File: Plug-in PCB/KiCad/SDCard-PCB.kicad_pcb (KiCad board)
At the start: 6 copper layers, 43 x 40 mm, 74 parts, among them J1 Conn_Coaxial, J10 Conn_01x01, J11 Conn_01x01, J14 Conn_01x01, J15 Conn_01x08, J16 Conn_01x01, J18 Conn_01x08, J2 Conn_01x01, J3 Conn_01x01, J4 Conn_01x01, J5 Conn_01x01, J6 Conn_01x01, J7 Conn_01x01, J8 Conn_01x01, J9 Conn_01x01, U1 DS90UB933-Q1, U2 TPS62402-Q1, U4 ATSAME70N21A-CN, Y1 ABM8G-12.000MHZ-4Y-T3

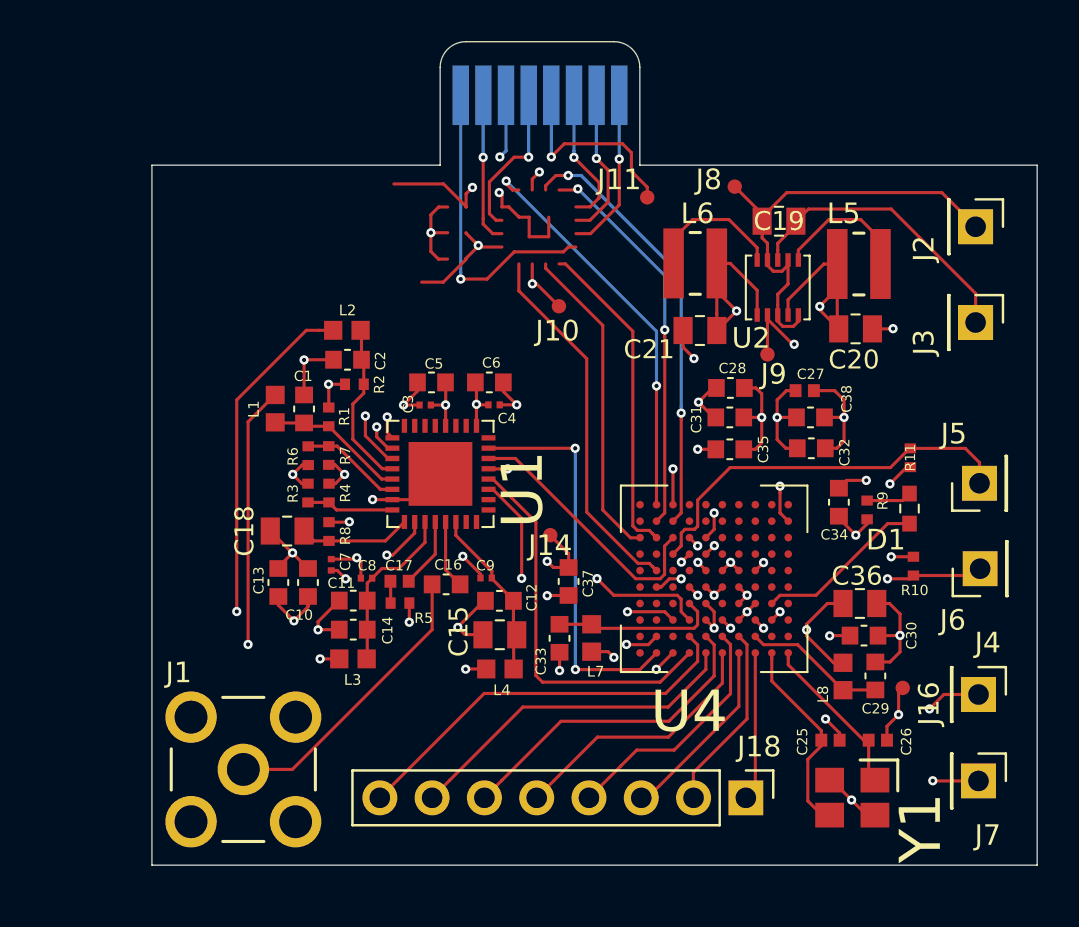
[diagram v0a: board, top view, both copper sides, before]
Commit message: Wired Expansion Board Update
1. Begin hardcoding bit-bang communication between wirefree MCU and wired expansion MCU.
++ Can I use the PIO module on the pins to send data in sync while grabbing image from the sensor with parallel capture mode?

2. Wired expansion board schematics and layout modifications
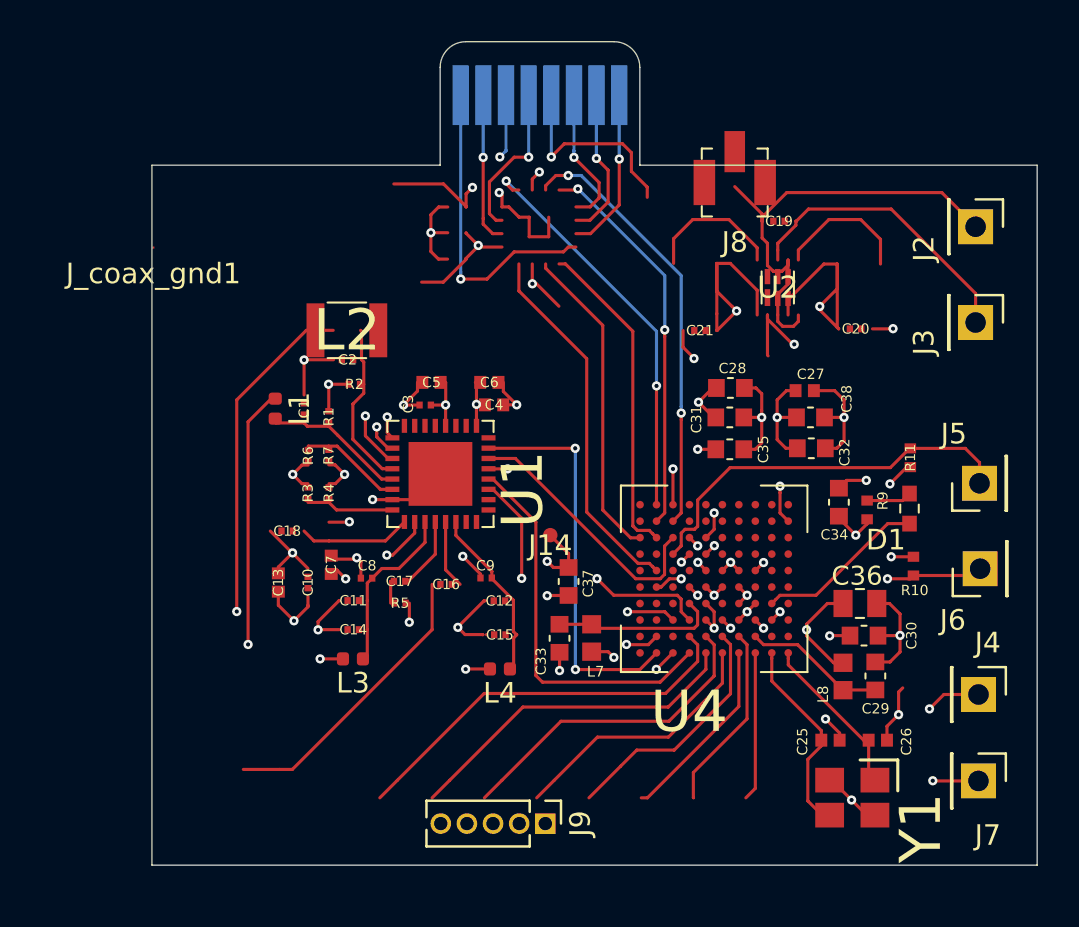
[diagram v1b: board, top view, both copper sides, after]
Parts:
- removed J1: Conn_Coaxial, .Connector:SMA-J-P-H-RA-TH1
- removed J10, J11, J16: Conn_01x01, .Connector:Conn_1x1_700_Circular_Pad
- removed J18: Conn_01x08, Connector_PinHeader_2.54mm:PinHeader_1x08_P2.54mm_Vertical
- removed L5, L6: VLS3012HBX-2R2M, .Inductor:VLS3012HBX-2R2M
- removed R8: 10k, .Resistor:R_0402_1005Metric_ERJ_L
- added J_coax_gnd1: Conn_01x01, .Connector:Conn_1x1_100x100_Pad, F.Cu at (100.1, 57.0)
- C1: value GQM1875C2E101JB12D -> GRM033R61A104ME15D; footprint .Capacitor:C_0603_1608Metric_L -> .Capacitor:C_0201_0603Metric_L
- C10, C11, C12: value GCJ188R71E104KA12D -> GRM033R61A104ME15D; footprint .Capacitor:C_0603_1608Metric_L -> .Capacitor:C_0201_0603Metric_L
- C13: value GRM188R61E475KE11D -> GRM155R60J106ME15D; footprint .Capacitor:C_0603_1608Metric_L -> .Capacitor:C_0402_1005Metric_L
- C14: value GRM188R61E475KE11D -> GRM033R71A103KA01D; footprint .Capacitor:C_0603_1608Metric_L -> .Capacitor:C_0201_0603Metric_L
- C15: value GRM21BR61C226ME44L -> GRM033R71A103KA01D; footprint .Capacitor:C_0805_2012Metric_L -> .Capacitor:C_0201_0603Metric_L
- C16: value GCJ188R71E104KA12D -> GRM033R71A103KA01D; footprint .Capacitor:C_0603_1608Metric_L -> .Capacitor:C_0201_0603Metric_L
- C17: value GRM155R71E473KA88D -> GRM033R71A103KA01D; footprint .Capacitor:C_0402_1005Metric_L -> .Capacitor:C_0201_0603Metric_L
- C18: value GCM21BR71E105KA56L -> GRM033R71A103KA01D; footprint .Capacitor:C_0805_2012Metric_L -> .Capacitor:C_0201_0603Metric_L
- C19: value GRM21BR61E106MA73L -> GRM033R61A105ME15D; footprint .Capacitor:C_0805_2012Metric_L -> .Capacitor:C_0201_0603Metric_L
- C2: value GQM1875C2E101JB12D -> GRM033R61C473KE84D; footprint .Capacitor:C_0603_1608Metric_L -> .Capacitor:C_0201_0603Metric_L
- C20, C21: value GRM21BR61C226ME44L -> GRM033R61A105ME15D; footprint .Capacitor:C_0805_2012Metric_L -> .Capacitor:C_0201_0603Metric_L
- C3: value GRM033R71A103KA01D -> GRM033R61A105ME15D
- C4: value GRM033R71A103KA01D -> GRM155R60J475ME47D; footprint .Capacitor:C_0201_0603Metric_L -> .Capacitor:C_0402_1005Metric_L
- C5: value GCJ188R71E104KA12D -> GRM155R60J475ME47D; footprint .Capacitor:C_0603_1608Metric_L -> .Capacitor:C_0402_1005Metric_L
- C6: value GCJ188R71E104KA12D -> GRJ155R60J106ME11D; footprint .Capacitor:C_0603_1608Metric_L -> .Capacitor:C_0402_1005Metric_L
- C7: value GRM033R71A103KA01D -> GRM155R60J106ME15D; footprint .Capacitor:C_0201_0603Metric_L -> .Capacitor:C_0402_1005Metric_L
- C8, C9: value GRM033R71A103KA01D -> GRM033R61A104ME15D
- J8: value Conn_01x01 -> Conn_Coaxial; footprint .Connector:Conn_1x1_700_Circular_Pad -> .Connector:U_FL-R-SMT_10_
- J9: value Conn_01x01 -> Conn_01x05; footprint .Connector:Conn_1x1_700_Circular_Pad -> Connector_PinHeader_1.27mm:PinHeader_1x05_P1.27mm_Vertical
- L1, L3, L4: value 1k @ 100MHz -> BLM15HD102SN1D; footprint .Inductor:L_0603_1608Metric_L -> Inductor_SMD:L_0402_1005Metric
- L2: value 1k @ 100MHz -> ADL3225V-470MT-TL000; footprint .Inductor:L_0603_1608Metric_L -> .Inductor:L_1210_3225Metric_L
- R1: value 4.7k -> ERJ-1GEF49R9C; footprint .Resistor:R_0402_1005Metric_ERJ_L -> .Resistor:R_0201_0603Metric_ERJ_L
- R2: value 4.7k -> ERJ-1GEF3321C; footprint .Resistor:R_0402_1005Metric_ERJ_L -> .Resistor:R_0201_0603Metric_ERJ_L
- R3: value 10 -> ERJ-1GEF1002C; footprint .Resistor:R_0402_1005Metric_ERJ_L -> .Resistor:R_0201_0603Metric_ERJ_L
- R4: value 50 or 4.7 -> ERJ-1GEF1003C; footprint .Resistor:R_0402_1005Metric_ERJ_L -> .Resistor:R_0201_0603Metric_ERJ_L
- R5: value 50 -> ERJ-1GEF1002C; footprint .Resistor:R_0402_1005Metric_ERJ_L -> .Resistor:R_0201_0603Metric_ERJ_L
- R6: value open -> ERJ-1GEF3321C; footprint .Resistor:R_0402_1005Metric_ERJ_L -> .Resistor:R_0201_0603Metric_ERJ_L
- R7: value 0 -> MMBT3904LP-7B; footprint .Resistor:R_0402_1005Metric_ERJ_L -> .Resistor:R_0201_0603Metric_ERJ_L
- U2: value TPS62402-Q1 -> TLV7103318DSER; footprint .Package_SON:SON_10_P50_300X300X100L40X24L -> .Package_SON:SON_6_P50_150X150X80L50X25L
- moved J9 25.2 mm to (119.1, 85.0), turned to 270 degrees
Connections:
- net /OnBoardMCU/CLK_OUT renamed Net-(U4-PadJ3)
- net /OnBoardMCU/IR_Receiver renamed Net-(U4-PadC1)
- net /OnBoardMCU/LED_PWM renamed Net-(U4-PadD8)
- net /OnBoardMCU/MONITOR0 renamed Net-(U4-PadG2)
- net /OnBoardMCU/NRESET renamed Net-(U4-PadG10)
- net /OnBoardMCU/RESET_N renamed Net-(U4-PadE2)
- net /OnBoardMCU/TRIGGER0 renamed Net-(U4-PadH1)
- net /OnBoardMCU/img_d6 renamed Net-(U4-PadK10)
- net /OnBoardMCU/img_d7 renamed Net-(U4-PadG5)
- net Net-(R3-Pad2) renamed /Serializer/MODE
- net Net-(U1-Pad24) renamed /Serializer/IMG_out5
- net Net-(U1-Pad26) renamed /Serializer/IMG_out6
- net Net-(U1-Pad27) renamed /Serializer/IMG_out7
- net Net-(U4-PadB10) renamed /OnBoardMCU/img_out3
- net Net-(U4-PadE10) renamed /OnBoardMCU/img_out0
- net Net-(U4-PadE8) renamed /OnBoardMCU/img_out1
- net Net-(U4-PadF10) renamed /OnBoardMCU/img_out2
- net Net-(U4-PadG9) renamed /OnBoardMCU/img_out4
- net Net-(U4-PadJ10) renamed /OnBoardMCU/img_out5
- net Net-(U4-PadK4) renamed /OnBoardMCU/img_out7
- net Net-(U4-PadK6) renamed /OnBoardMCU/img_out6
- C1 pad 1: Net-(C1-Pad1) -> /Serializer/DOUT_P
- C1 pad 2: Earth -> Net-(C1-Pad2)
- C10 pad 1: +1V8 -> /Serializer/VDDCML
- C10 pad 2: Earth -> GND
- C11 pad 1: Net-(C11-Pad1) -> +1V8
- C11 pad 2: Earth -> GND
- C12 pad 1: Net-(C12-Pad1) -> +1V8
- C12 pad 2: Earth -> GND
- C13 pad 1: +1V8 -> +5V
- C13 pad 2: Earth -> GND
- C14 pad 1: Net-(C11-Pad1) -> +1V8
- C14 pad 2: Earth -> GND
- C15 pad 1: Net-(C12-Pad1) -> /Serializer/VDDPLL
- C15 pad 2: Earth -> GND
- C16 pad 1: Net-(C16-Pad1) -> /Serializer/VDDCML
- C16 pad 2: Net-(C16-Pad2) -> GND
- C17 pad 1: Net-(C17-Pad1) -> +1V8
- C17 pad 2: Net-(C17-Pad2) -> GND
- C18 pad 1: Net-(C18-Pad1) -> +1V8
- C18 pad 2: Earth -> GND
- C19 pad 1: +BATT -> +5V
- C19 pad 2: Earth -> GND
- C2 pad 2: Earth -> Net-(C2-Pad2)
- C20 pad 2: Earth -> GND
- C21 pad 2: Earth -> GND
- C3 pad 1: +1V8 -> /Serializer/PDB
- C3 pad 2: Earth -> GND
- C4 pad 1: +3V3 -> +1V8
- C4 pad 2: Earth -> GND
- C5 pad 1: +1V8 -> /Serializer/VDDPLL
- C5 pad 2: Earth -> GND
- C6 pad 1: +3V3 -> /Serializer/VDDCML
- C6 pad 2: Earth -> GND
- C7 pad 1: +1V8 -> +5V
- C7 pad 2: Earth -> GND
- C8 pad 1: Net-(C11-Pad1) -> +1V8
- C8 pad 2: Earth -> GND
- C9 pad 1: Net-(C12-Pad1) -> /Serializer/VDDPLL
- C9 pad 2: Earth -> GND
- J15 pad 1: /SD_Input/DAT2 -> /SD_Input/SD_in2
- J15 pad 2: /SD_Input/DAT3 -> /SD_Input/SD_in3
- J15 pad 3: /SD_Input/SDCardCMDA -> /SD_Input/WXB_CMD
- J15 pad 4: +3V3 -> Net-(J15-Pad4)
- J15 pad 5: /SD_Input/SDCardCLKA -> /SD_Input/WXB_CLK
- J15 pad 7: /SD_Input/DAT0 -> /SD_Input/SD_in0
- J15 pad 8: /SD_Input/DAT1 -> /SD_Input/SD_in1
- J8 pad 1: +BATT -> /Serializer/DOUT_P
- J9 pad 1: Earth -> /OnBoardMCU/test1
- L1 pad 1: /OnBoardMCU/SDA -> /Serializer/DOUT_P
- L1 pad 2: Net-(C1-Pad1) -> Net-(L1-Pad2)
- L2 pad 1: /OnBoardMCU/SCL -> Net-(L1-Pad2)
- L2 pad 2: Net-(C2-Pad1) -> +5V
- L3 pad 1: Net-(C11-Pad1) -> /Serializer/VDDPLL
- L4 pad 1: Net-(C12-Pad1) -> /Serializer/VDDCML
- R1 pad 1: +1V8 -> GND
- R1 pad 2: Net-(C1-Pad1) -> Net-(C2-Pad1)
- R2 pad 1: +1V8 -> +3V3
- R2 pad 2: Net-(C2-Pad1) -> /OnBoardMCU/SCL
- R4 pad 2: Earth -> GND
- R5 pad 1: Net-(C17-Pad1) -> +1V8
- R5 pad 2: Earth -> /Serializer/PDB
- R6 pad 1: +1V8 -> +3V3
- R6 pad 2: Net-(R6-Pad2) -> /OnBoardMCU/SDA
- R7 pad 1: Net-(R6-Pad2) -> +5V
- R7 pad 2: Earth -> Net-(L1-Pad2)
- U1 pad 10: +1V8 -> /Serializer/VDDPLL
- U1 pad 11: Net-(C11-Pad1) -> +1V8
- U1 pad 12: Net-(C17-Pad2) -> Net-(C2-Pad2)
- U1 pad 13: Net-(C16-Pad2) -> Net-(C1-Pad2)
- U1 pad 14: Net-(C12-Pad1) -> /Serializer/VDDCML
- U1 pad 18: Net-(U1-Pad18) -> /OnBoardMCU/SER_CLK
- U1 pad 19: /OnBoardMCU/SD_out0 -> /Serializer/IMG_out0
- U1 pad 20: /OnBoardMCU/SD_out1 -> /Serializer/IMG_out1
- U1 pad 21: /OnBoardMCU/SD_out2 -> /Serializer/IMG_out2
- U1 pad 22: /OnBoardMCU/SD_out3 -> /Serializer/IMG_out3
- U1 pad 23: /OnBoardMCU/SD_CMD -> /Serializer/IMG_out4
- U1 pad 25: +3V3 -> +1V8
- U1 pad 3: /OnBoardMCU/SD_CLK -> /OnBoardMCU/PXL_CLK
- U1 pad 33: Earth -> GND
- U1 pad 4: Net-(C2-Pad1) -> /OnBoardMCU/SCL
- U1 pad 5: Net-(C1-Pad1) -> /OnBoardMCU/SDA
- U1 pad 6: Net-(R6-Pad2) -> GND
- U1 pad 7: Earth -> GND
- U1 pad 9: Net-(C18-Pad1) -> /Serializer/PDB
- U2 pad 1: +3V3 -> +5V
- U2 pad 2: Earth -> +5V
- U2 pad 3: +BATT -> +5V
- U2 pad 4: +1V8 -> GND
- U2 pad 5: +BATT -> +1V8
- U2 pad 6: Net-(L5-Pad1) -> +3V3
- U4 pad A3: /OnBoardMCU/test1 -> Net-(U4-PadA3)
- U4 pad A4: /OnBoardMCU/test3 -> Net-(U4-PadA4)
- U4 pad A5: /OnBoardMCU/test5 -> /OnBoardMCU/test2
- U4 pad A6: /OnBoardMCU/test7 -> /OnBoardMCU/test4
- U4 pad A7: /OnBoardMCU/SD_out1 -> Net-(U4-PadA7)
- U4 pad A9: /OnBoardMCU/SD_CMD -> Net-(U4-PadA9)
- U4 pad B4: /OnBoardMCU/test2 -> Net-(U4-PadB4)
- U4 pad B5: /OnBoardMCU/test4 -> /OnBoardMCU/test1
- U4 pad B6: /OnBoardMCU/test6 -> /OnBoardMCU/test3
- U4 pad B7: /OnBoardMCU/test8 -> /OnBoardMCU/test5
- U4 pad C7: /OnBoardMCU/SD_out0 -> Net-(U4-PadC7)
- U4 pad F9: /SD_Input/DAT0 -> /OnBoardMCU/SD_in0
- U4 pad G1: /OnBoardMCU/CLOCK -> /OnBoardMCU/SER_CLK
- U4 pad G4: Net-(U4-PadG4) -> /OnBoardMCU/PXL_CLK
- U4 pad H10: /SD_Input/DAT1 -> /OnBoardMCU/SD_in1
- U4 pad H5: Net-(U4-PadH5) -> /OnBoardMCU/LINE_VALID
- U4 pad H6: /OnBoardMCU/FRAME_VALID -> /OnBoardMCU/WXB_inCLK
- U4 pad H7: /OnBoardMCU/SD_CLK -> Net-(U4-PadH7)
- U4 pad H8: /OnBoardMCU/SD_out3 -> Net-(U4-PadH8)
- U4 pad H9: /SD_Input/DAT2 -> /OnBoardMCU/SD_in2
- U4 pad J1: /OnBoardMCU/LINE_VALID -> Net-(U4-PadJ1)
- U4 pad J4: Net-(U4-PadJ4) -> /OnBoardMCU/FRAME_VALID
- U4 pad J8: /SD_Input/SDCardCMDA -> Net-(U4-PadJ8)
- U4 pad J9: /SD_Input/DAT3 -> /OnBoardMCU/SD_in3
- U4 pad K8: /OnBoardMCU/SD_out2 -> Net-(U4-PadK8)
- U4 pad K9: /SD_Input/SDCardCLKA -> /OnBoardMCU/WXB_inCMD
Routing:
- net /SD_Input/DAT1: track 30.6 -> 0.00 mm, vias 1 -> 0
- net /SD_Input/SDCardCMDA: track 27.9 -> 0.00 mm, vias 3 -> 0
- net /SD_Input/SDCardCLKA: track 27.3 -> 0.00 mm, vias 3 -> 0
- net /SD_Input/DAT3: track 26.4 -> 0.00 mm, vias 3 -> 0
- net /SD_Input/DAT0: track 25.4 -> 0.00 mm, vias 1 -> 0
- net /SD_Input/DAT2: track 23.8 -> 0.00 mm, vias 1 -> 0
- net Net-(U4-PadJ8): track 0.00 -> 21.1 mm, vias 0 -> 2
- net /OnBoardMCU/WXB_inCMD: track 0.00 -> 19.6 mm, vias 0 -> 2
- net /OnBoardMCU/test8: track 19.6 -> 0.00 mm
- net /OnBoardMCU/SD_in3: track 0.00 -> 19.0 mm, vias 0 -> 2
- net +1V8: track 51.3 -> 33.2 mm, vias 23 -> 18
- net /OnBoardMCU/SD_in0: track 0.00 -> 18.0 mm
- net GND: track 0.00 -> 16.7 mm, vias 0 -> 5
- net /OnBoardMCU/test7: track 16.7 -> 0.00 mm
- net /OnBoardMCU/SD_in2: track 0.00 -> 15.8 mm
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
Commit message: Wired Expansion Board Updates
1. KiCad: Schematics and layouts completed/Gerber files generated
2. Atmel: Communication protocol from WireFree to WiredExpansion written
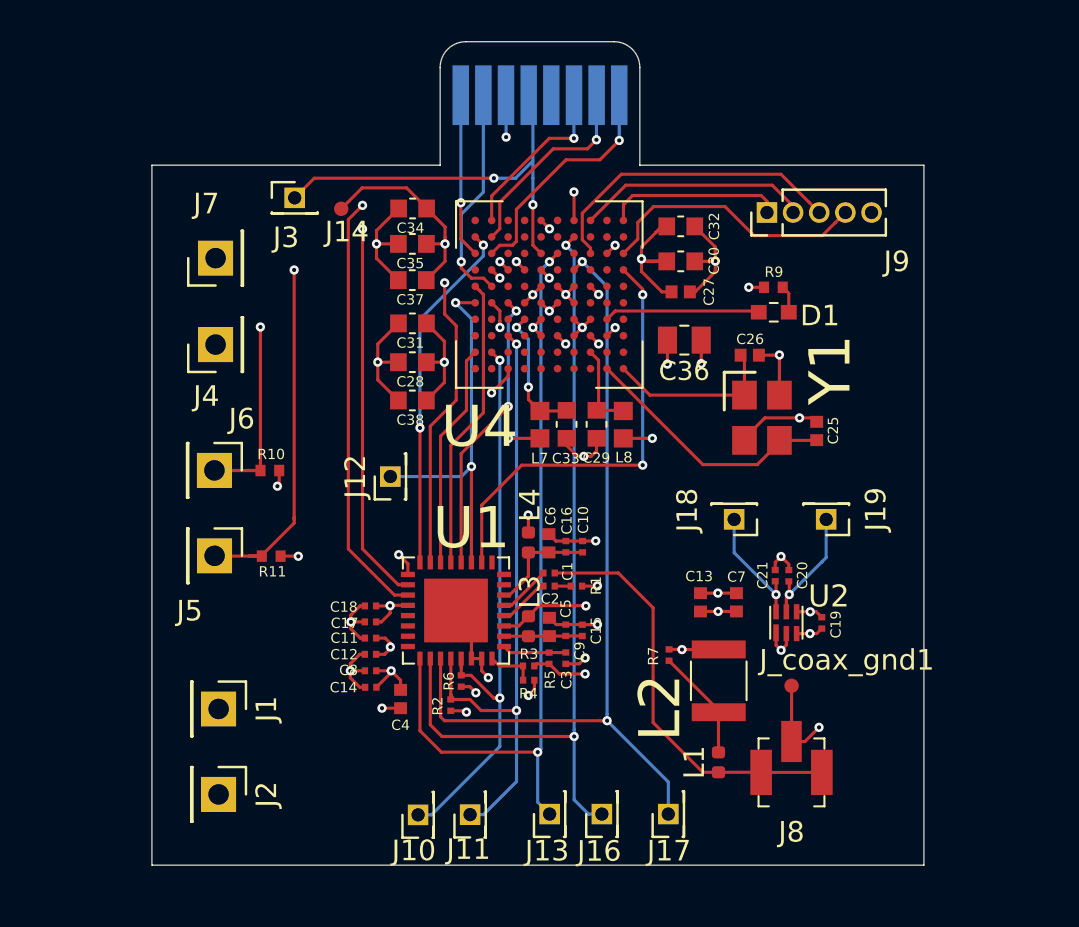
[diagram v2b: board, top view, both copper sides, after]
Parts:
- added J1: Conn_01x01, Connector_PinHeader_2.54mm:PinHeader_1x01_P2.54mm_Vertical, F.Cu at (103.2, 79.4)
- added J10: Conn_01x01, Connector_PinHeader_1.27mm:PinHeader_1x01_P1.27mm_Vertical, F.Cu at (112.9, 84.6)
- added J11: Conn_01x01, Connector_PinHeader_1.27mm:PinHeader_1x01_P1.27mm_Vertical, F.Cu at (115.5, 84.5)
- added J12: Conn_01x01, Connector_PinHeader_1.27mm:PinHeader_1x01_P1.27mm_Vertical, F.Cu at (111.6, 68.1)
- added J13: Conn_01x01, Connector_PinHeader_1.27mm:PinHeader_1x01_P1.27mm_Vertical, F.Cu at (119.3, 84.5)
- added J16: Conn_01x01, Connector_PinHeader_1.27mm:PinHeader_1x01_P1.27mm_Vertical, F.Cu at (121.9, 84.5)
- added J17: Conn_01x01, Connector_PinHeader_1.27mm:PinHeader_1x01_P1.27mm_Vertical, F.Cu at (125.1, 84.5)
- added J18: Conn_01x01, Connector_PinHeader_1.27mm:PinHeader_1x01_P1.27mm_Vertical, F.Cu at (128.3, 70.2)
- added J19: Conn_01x01, Connector_PinHeader_1.27mm:PinHeader_1x01_P1.27mm_Vertical, F.Cu at (132.8, 70.2)
- J3: footprint Connector_PinHeader_2.54mm:PinHeader_1x01_P2.54mm_Vertical -> Connector_PinHeader_1.27mm:PinHeader_1x01_P1.27mm_Vertical
- J_coax_gnd1: footprint .Connector:Conn_1x1_100x100_Pad -> .Connector:Conn_1x1_700_Circular_Pad
- moved J2 46.0 mm to (103.2, 83.6)
- moved J7 44.9 mm to (103.1, 57.5), turned to 90 degrees
- moved J4 40.8 mm to (103.1, 61.7), turned to 90 degrees
- moved J_coax_gnd1 37.6 mm to (131.1, 78.3), turned to 180 degrees
- moved J6 37.5 mm to (103.0, 67.8), turned to 270 degrees
- moved J5 37.3 mm to (103.0, 72.0), turned to 270 degrees
- moved J3 33.6 mm to (106.9, 54.6), turned to 0 degrees
- moved R10 31.6 mm to (105.7, 67.8), turned to 180 degrees
- moved J9 31.6 mm to (129.9, 55.3), turned to 90 degrees
- moved R11 31.4 mm to (105.8, 72.0), turned to 180 degrees
- moved J8 28.8 mm to (131.1, 82.7)
- moved L1 27.5 mm to (127.5, 82.0), turned to 90 degrees
- moved C34 25.1 mm to (112.7, 55.1), turned to 180 degrees
- moved L2 24.8 mm to (127.5, 78.0), turned to 90 degrees
- moved C13 20.5 mm to (126.6, 74.2)
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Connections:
- C10 pad 2: GND -> Earth
- C11 pad 2: GND -> Earth
- C12 pad 2: GND -> Earth
- C13 pad 2: GND -> Earth
- C14 pad 2: GND -> Earth
- C15 pad 2: GND -> Earth
- C16 pad 2: GND -> Earth
- C17 pad 2: GND -> Earth
- C18 pad 2: GND -> Earth
- C19 pad 2: GND -> Earth
- C20 pad 2: GND -> Earth
- C21 pad 2: GND -> Earth
- C3 pad 2: GND -> Earth
- C4 pad 2: GND -> Earth
- C5 pad 2: GND -> Earth
- C6 pad 2: GND -> Earth
- C7 pad 2: GND -> Earth
- C8 pad 2: GND -> Earth
- C9 pad 2: GND -> Earth
- J15 pad 1: /SD_Input/SD_in2 -> /OnBoardMCU/WXB_in2
- J15 pad 2: /SD_Input/SD_in3 -> /OnBoardMCU/WXB_in3
- J15 pad 3: /SD_Input/WXB_CMD -> /OnBoardMCU/WXB_CMD
- J15 pad 5: /SD_Input/WXB_CLK -> /OnBoardMCU/WXB_CLK
- J15 pad 7: /SD_Input/SD_in0 -> /OnBoardMCU/WXB_in0
- J15 pad 8: /SD_Input/SD_in1 -> /OnBoardMCU/WXB_in1
- J2 pad 1: +BATT -> +1V8
- J3 pad 1: Earth -> /OnBoardMCU/WXB_CLK
- J8 pad 2: GND -> Earth
- J_coax_gnd1 pad 1: GND -> Earth
- R1 pad 1: GND -> Earth
- R4 pad 2: GND -> Earth
- U1 pad 19: /Serializer/IMG_out0 -> /OnBoardMCU/IMG_out0
- U1 pad 20: /Serializer/IMG_out1 -> /OnBoardMCU/IMG_out1
- U1 pad 21: /Serializer/IMG_out2 -> /OnBoardMCU/IMG_out2
- U1 pad 22: /Serializer/IMG_out3 -> /OnBoardMCU/IMG_out3
- U1 pad 23: /Serializer/IMG_out4 -> /OnBoardMCU/IMG_out4
- U1 pad 24: /Serializer/IMG_out5 -> /OnBoardMCU/IMG_out5
- U1 pad 26: /Serializer/IMG_out6 -> /OnBoardMCU/IMG_out6
- U1 pad 27: /Serializer/IMG_out7 -> /OnBoardMCU/IMG_out7
- U1 pad 33: GND -> Earth
- U1 pad 6: GND -> Earth
- U1 pad 7: GND -> Earth
- U2 pad 4: GND -> Earth
- U4 pad A5: /OnBoardMCU/test2 -> Net-(U4-PadA5)
- U4 pad A6: /OnBoardMCU/test4 -> Net-(U4-PadA6)
- U4 pad B10: /OnBoardMCU/img_out3 -> /OnBoardMCU/IMG_out3
- U4 pad B5: /OnBoardMCU/test1 -> Net-(U4-PadB5)
- U4 pad B6: /OnBoardMCU/test3 -> Net-(U4-PadB6)
- U4 pad B7: /OnBoardMCU/test5 -> Net-(U4-PadB7)
- U4 pad E10: /OnBoardMCU/img_out0 -> /OnBoardMCU/IMG_out0
- U4 pad E8: /OnBoardMCU/img_out1 -> /OnBoardMCU/IMG_out1
- U4 pad F10: /OnBoardMCU/img_out2 -> /OnBoardMCU/IMG_out2
- U4 pad F9: /OnBoardMCU/SD_in0 -> /OnBoardMCU/WXB_in0
- U4 pad G9: /OnBoardMCU/img_out4 -> /OnBoardMCU/IMG_out4
- U4 pad H1: Net-(U4-PadH1) -> /OnBoardMCU/test4
- U4 pad H10: /OnBoardMCU/SD_in1 -> /OnBoardMCU/WXB_in1
- U4 pad H2: Net-(U4-PadH2) -> /OnBoardMCU/test5
- U4 pad H3: Net-(U4-PadH3) -> /OnBoardMCU/test3
- U4 pad H6: /OnBoardMCU/WXB_inCLK -> /OnBoardMCU/WXB_CLK
- U4 pad H9: /OnBoardMCU/SD_in2 -> /OnBoardMCU/WXB_in2
- U4 pad J10: /OnBoardMCU/img_out5 -> /OnBoardMCU/IMG_out5
- U4 pad J9: /OnBoardMCU/SD_in3 -> /OnBoardMCU/WXB_in3
- U4 pad K1: Net-(U4-PadK1) -> /OnBoardMCU/test1
- U4 pad K3: Net-(U4-PadK3) -> /OnBoardMCU/test2
- U4 pad K4: /OnBoardMCU/img_out7 -> /OnBoardMCU/IMG_out7
- U4 pad K6: /OnBoardMCU/img_out6 -> /OnBoardMCU/IMG_out6
- U4 pad K9: /OnBoardMCU/WXB_inCMD -> /OnBoardMCU/WXB_CMD
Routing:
- net /OnBoardMCU/PXL_CLK: track 0.00 -> 40.1 mm, vias 0 -> 2
- net /OnBoardMCU/IMG_out7: track 0.00 -> 32.7 mm, vias 0 -> 2
- net /OnBoardMCU/IMG_out6: track 0.00 -> 28.1 mm, vias 0 -> 2
- net /OnBoardMCU/SD_CLK: track 22.8 -> 0.00 mm, vias 2 -> 0
- net Earth: track 86.5 -> 64.0 mm, vias 27 -> 26
- net +BATT: track 22.4 -> 0.00 mm
- net /OnBoardMCU/SER_CLK: track 0.00 -> 21.3 mm, vias 0 -> 2
- net Net-(U4-PadJ8): track 21.1 -> 0.00 mm, vias 2 -> 0
- net /Serializer/DOUT_P: track 0.00 -> 20.3 mm
- net /OnBoardMCU/WXB_CLK: track 0.00 -> 20.2 mm, vias 0 -> 2
- net /OnBoardMCU/WXB_inCMD: track 19.6 -> 0.00 mm, vias 2 -> 0
- net /OnBoardMCU/SD_CMD: track 19.2 -> 0.00 mm, vias 2 -> 0
- net /OnBoardMCU/SD_in3: track 19.0 -> 0.00 mm, vias 2 -> 0
- net /OnBoardMCU/SD_out1: track 18.8 -> 0.00 mm
- net /OnBoardMCU/FRAME_VALID: track 21.1 -> 39.7 mm
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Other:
- board size 43 x 40 mm -> 37.5 x 40 mm

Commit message: Change WXB to 4-layer
1. Change the WXB to 4 layers
2. Change board thickness to 1mm
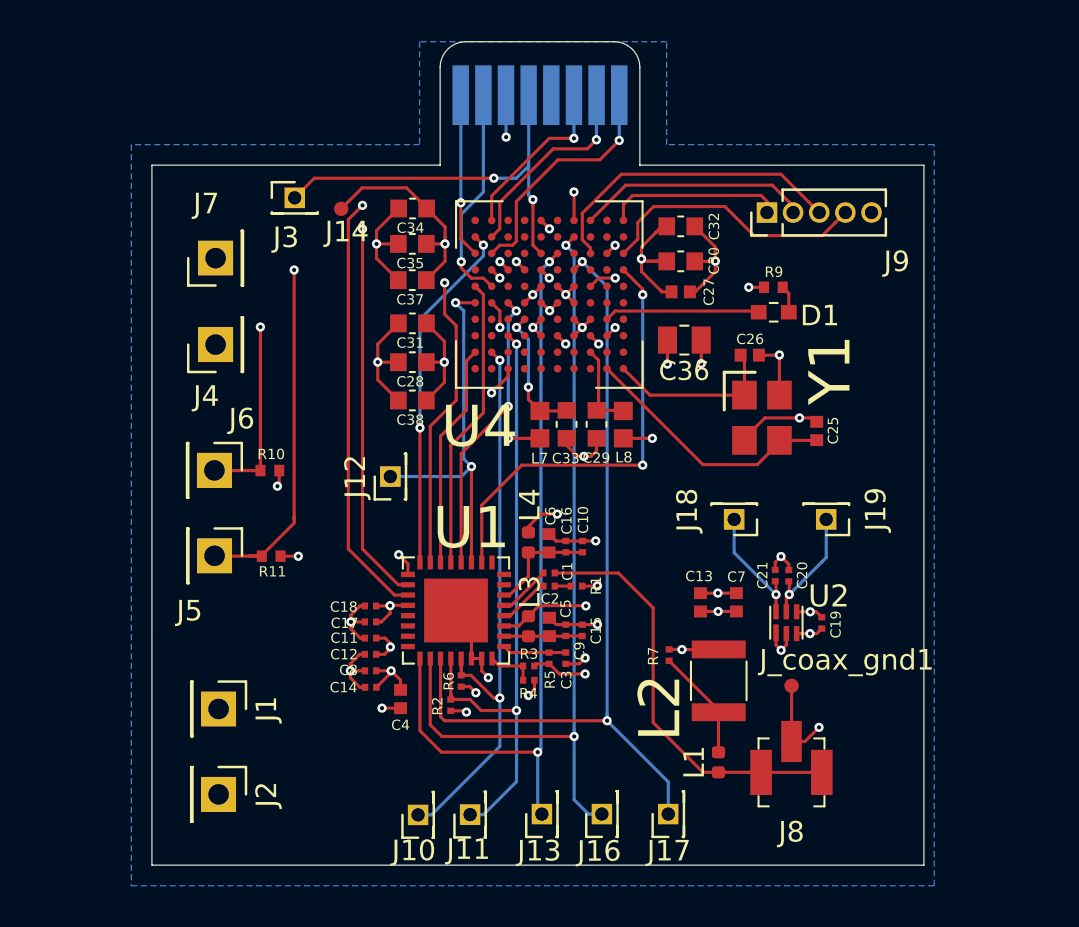
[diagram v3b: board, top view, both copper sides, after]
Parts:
- moved J13 0.38 mm to (118.9, 84.5)
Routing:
- net +1V8: track 40.8 -> 42.7 mm
- added copper zone on In2.Cu, net +1V2
- added copper zone on B.Cu, net +1V8
- added copper zone on In2.Cu, net +3V3
- removed copper zone on In3.Cu, net +1V2
- removed copper zone on In4.Cu, net +1V8
- removed copper zone on In3.Cu, net +3V3
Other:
- copper layers 6 -> 4
